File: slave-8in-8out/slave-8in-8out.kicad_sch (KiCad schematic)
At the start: 47 parts, among them J1 Conn_01x06_Male, J2 Screw_Terminal_01x02, J3 Conn_01x06_Female, J4 Screw_Terminal_01x04, J5 Screw_Terminal_01x04, J6 Screw_Terminal_01x04, J7 Screw_Terminal_01x04, J8 Conn_01x10_Female, J9 Screw_Terminal_01x02, SW1 SW_DIP_x03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

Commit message: update slave-8in-8out routing
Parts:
- D1, D2, D3, D4, D5, D6, D7, D8: footprint Resistor_SMD:R_0805_2012Metric -> LED_SMD:LED_0805_2012Metric
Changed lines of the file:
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@@
     (property "Reference" "D1" (id 0) (at 127.381 85.09 0))
     (property "Value" "LED" (id 1) (at 127.381 87.63 0))
-    (property "Footprint" "Resistor_SMD:R_0805_2012Metric" (id 2) (at 127 92.71 0)
+    (property "Footprint" "LED_SMD:LED_0805_2012Metric" (id 2) (at 127 92.71 0)
       (effects (font (size 1.27 1.27)) hide)
     )
@@
     (property "Reference" "D2" (id 0) (at 127.381 93.98 0))
     (property "Value" "LED" (id 1) (at 127.381 96.52 0))
-    (property "Footprint" "Resistor_SMD:R_0805_2012Metric" (id 2) (at 127 101.6 0)
+    (property "Footprint" "LED_SMD:LED_0805_2012Metric" (id 2) (at 127 101.6 0)
       (effects (font (size 1.27 1.27)) hide)
     )
@@
     (property "Reference" "D3" (id 0) (at 127.381 102.87 0))
     (property "Value" "LED" (id 1) (at 127.381 105.41 0))
-    (property "Footprint" "Resistor_SMD:R_0805_2012Metric" (id 2) (at 127 110.49 0)
+    (property "Footprint" "LED_SMD:LED_0805_2012Metric" (id 2) (at 127 110.49 0)
       (effects (font (size 1.27 1.27)) hide)
     )
@@
     (property "Reference" "D4" (id 0) (at 127.381 111.76 0))
     (property "Value" "LED" (id 1) (at 127.381 114.3 0))
-    (property "Footprint" "Resistor_SMD:R_0805_2012Metric" (id 2) (at 127 119.38 0)
+    (property "Footprint" "LED_SMD:LED_0805_2012Metric" (id 2) (at 127 119.38 0)
       (effects (font (size 1.27 1.27)) hide)
     )
@@
     (property "Reference" "D5" (id 0) (at 127.381 120.65 0))
     (property "Value" "LED" (id 1) (at 127.381 123.19 0))
-    (property "Footprint" "Resistor_SMD:R_0805_2012Metric" (id 2) (at 127 128.27 0)
+    (property "Footprint" "LED_SMD:LED_0805_2012Metric" (id 2) (at 127 128.27 0)
       (effects (font (size 1.27 1.27)) hide)
     )
@@
     (property "Reference" "D6" (id 0) (at 127.381 129.54 0))
     (property "Value" "LED" (id 1) (at 127.381 132.08 0))
-    (property "Footprint" "Resistor_SMD:R_0805_2012Metric" (id 2) (at 127 137.16 0)
+    (property "Footprint" "LED_SMD:LED_0805_2012Metric" (id 2) (at 127 137.16 0)
       (effects (font (size 1.27 1.27)) hide)
     )
@@
     (property "Reference" "D7" (id 0) (at 127.381 138.43 0))
     (property "Value" "LED" (id 1) (at 127.381 140.97 0))
-    (property "Footprint" "Resistor_SMD:R_0805_2012Metric" (id 2) (at 127 146.05 0)
+    (property "Footprint" "LED_SMD:LED_0805_2012Metric" (id 2) (at 127 146.05 0)
       (effects (font (size 1.27 1.27)) hide)
     )
@@
     (property "Reference" "D8" (id 0) (at 127.381 147.32 0))
     (property "Value" "LED" (id 1) (at 127.381 149.86 0))
-    (property "Footprint" "Resistor_SMD:R_0805_2012Metric" (id 2) (at 127 154.94 0)
+    (property "Footprint" "LED_SMD:LED_0805_2012Metric" (id 2) (at 127 154.94 0)
       (effects (font (size 1.27 1.27)) hide)
     )
@@
     )
     (path "/1130ddb6-2676-4fcc-a4bc-f126e5a4cfda"
-      (reference "D1") (unit 1) (value "LED") (footprint "Resistor_SMD:R_0805_2012Metric")
+      (reference "D1") (unit 1) (value "LED") (footprint "LED_SMD:LED_0805_2012Metric")
     )
     (path "/c04a3c0f-1c24-409e-afcf-fa43ae33581a"
-      (reference "D2") (unit 1) (value "LED") (footprint "Resistor_SMD:R_0805_2012Metric")
+      (reference "D2") (unit 1) (value "LED") (footprint "LED_SMD:LED_0805_2012Metric")
     )
     (path "/05aa0f77-6513-48a5-a5d4-97e427a3a373"
-      (reference "D3") (unit 1) (value "LED") (footprint "Resistor_SMD:R_0805_2012Metric")
+      (reference "D3") (unit 1) (value "LED") (footprint "LED_SMD:LED_0805_2012Metric")
     )
     (path "/eaa25c40-d6da-42ff-9377-01443632b7c7"
-      (reference "D4") (unit 1) (value "LED") (footprint "Resistor_SMD:R_0805_2012Metric")
+      (reference "D4") (unit 1) (value "LED") (footprint "LED_SMD:LED_0805_2012Metric")
     )
     (path "/504d2596-392e-4876-87b1-2ae7254e5876"
-      (reference "D5") (unit 1) (value "LED") (footprint "Resistor_SMD:R_0805_2012Metric")
+      (reference "D5") (unit 1) (value "LED") (footprint "LED_SMD:LED_0805_2012Metric")
     )
     (path "/4c0f8732-eaad-43c0-94bc-9e71f4a27432"
-      (reference "D6") (unit 1) (value "LED") (footprint "Resistor_SMD:R_0805_2012Metric")
+      (reference "D6") (unit 1) (value "LED") (footprint "LED_SMD:LED_0805_2012Metric")
     )
     (path "/f4af2212-81b4-4a8c-a4ec-5b893151c71f"
-      (reference "D7") (unit 1) (value "LED") (footprint "Resistor_SMD:R_0805_2012Metric")
+      (reference "D7") (unit 1) (value "LED") (footprint "LED_SMD:LED_0805_2012Metric")
     )
     (path "/20c2455c-6d84-4646-a0f8-565d2e8a91c0"
-      (reference "D8") (unit 1) (value "LED") (footprint "Resistor_SMD:R_0805_2012Metric")
+      (reference "D8") (unit 1) (value "LED") (footprint "LED_SMD:LED_0805_2012Metric")
     )
     (path "/00000000-0000-0000-0000-0000601f3a35/b0a7a218-e2f0-4093-b668-da203b2eafe3"
-      (reference "D9") (unit 1) (value "LED") (footprint "Resistor_SMD:R_0805_2012Metric")
+      (reference "D9") (unit 1) (value "LED") (footprint "LED_SMD:LED_0805_2012Metric")
     )
     (path "/00000000-0000-0000-0000-0000601f3f45/b0a7a218-e2f0-4093-b668-da203b2eafe3"
-      (reference "D11") (unit 1) (value "LED") (footprint "Resistor_SMD:R_0805_2012Metric")
+      (reference "D11") (unit 1) (value "LED") (footprint "LED_SMD:LED_0805_2012Metric")
     )
     (path "/00000000-0000-0000-0000-0000601fb64e/b0a7a218-e2f0-4093-b668-da203b2eafe3"
-      (reference "D13") (unit 1) (value "LED") (footprint "Resistor_SMD:R_0805_2012Metric")
+      (reference "D13") (unit 1) (value "LED") (footprint "LED_SMD:LED_0805_2012Metric")
     )
     (path "/00000000-0000-0000-0000-0000601f54fa/b0a7a218-e2f0-4093-b668-da203b2eafe3"
-      (reference "D15") (unit 1) (value "LED") (footprint "Resistor_SMD:R_0805_2012Metric")
+      (reference "D15") (unit 1) (value "LED") (footprint "LED_SMD:LED_0805_2012Metric")
     )
     (path "/00000000-0000-0000-0000-0000601f5635/b0a7a218-e2f0-4093-b668-da203b2eafe3"
-      (reference "D17") (unit 1) (value "LED") (footprint "Resistor_SMD:R_0805_2012Metric")
+      (reference "D17") (unit 1) (value "LED") (footprint "LED_SMD:LED_0805_2012Metric")
     )
     (path "/00000000-0000-0000-0000-0000601f5761/b0a7a218-e2f0-4093-b668-da203b2eafe3"
-      (reference "D19") (unit 1) (value "LED") (footprint "Resistor_SMD:R_0805_2012Metric")
+      (reference "D19") (unit 1) (value "LED") (footprint "LED_SMD:LED_0805_2012Metric")
     )
     (path "/00000000-0000-0000-0000-0000601f5881/b0a7a218-e2f0-4093-b668-da203b2eafe3"
-      (reference "D21") (unit 1) (value "LED") (footprint "Resistor_SMD:R_0805_2012Metric")
+      (reference "D21") (unit 1) (value "LED") (footprint "LED_SMD:LED_0805_2012Metric")
     )
     (path "/00000000-0000-0000-0000-0000601f5cf2/b0a7a218-e2f0-4093-b668-da203b2eafe3"
-      (reference "D23") (unit 1) (value "LED") (footprint "Resistor_SMD:R_0805_2012Metric")
+      (reference "D23") (unit 1) (value "LED") (footprint "LED_SMD:LED_0805_2012Metric")
     )
     (path "/eee10ae1-7e56-41a5-a4ef-cb8260ee8633"

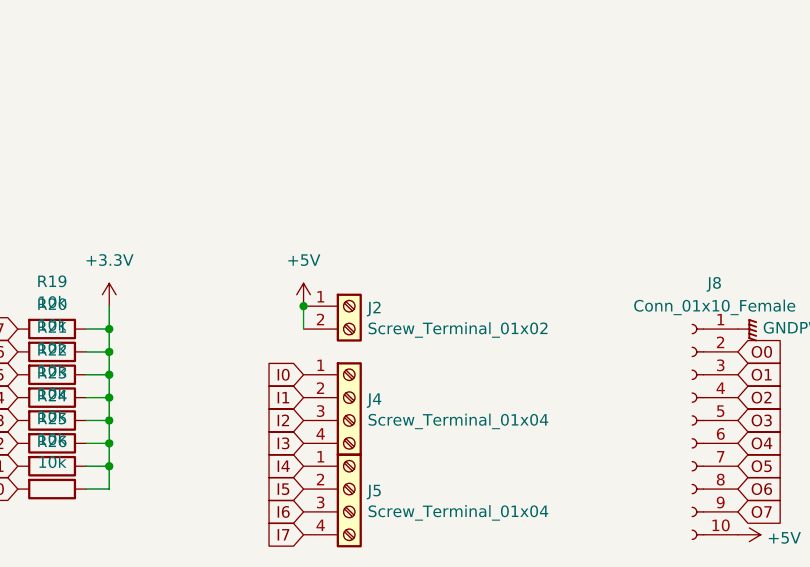
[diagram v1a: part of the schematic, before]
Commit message: update slave-8in-8out routing
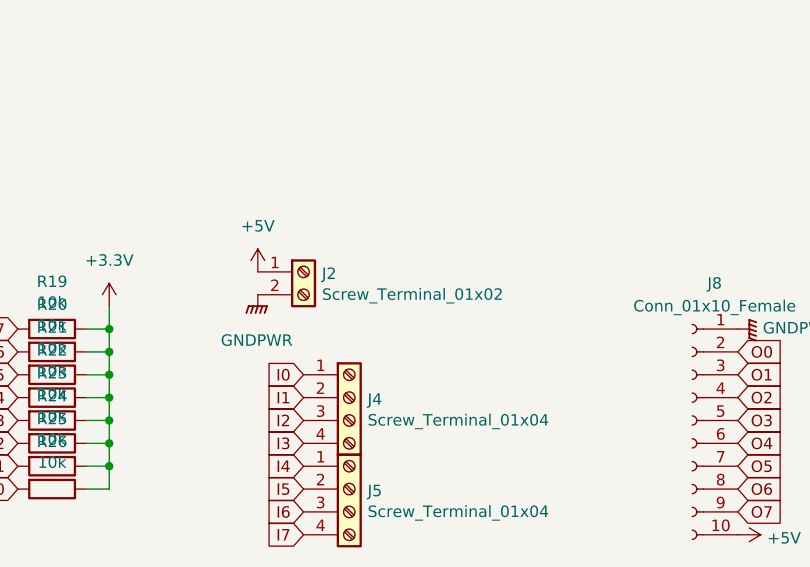
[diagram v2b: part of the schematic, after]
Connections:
- net +5V: no longer J2.2 (Pin_2)
- net GNDPWR: now also J2.2 (Pin_2)
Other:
- moved on the sheet: J2
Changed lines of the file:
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@@
   (junction (at 152.4 64.77) (diameter 0) (color 0 0 0 0))
   (junction (at 152.4 67.31) (diameter 0) (color 0 0 0 0))
-  (junction (at 173.99 49.53) (diameter 0.9144) (color 0 0 0 0))
   (no_connect (at 95.25 43.18))
   (wire (pts (xy 24.13 67.31) (xy 27.94 67.31))
@@
     (stroke (width 0) (type default) (color 0 0 0 0))
   )
-  (wire (pts (xy 173.99 49.53) (xy 173.99 52.07))
-    (stroke (width 0) (type solid) (color 0 0 0 0))
-  )
   (wire (pts (xy 173.99 91.44) (xy 176.53 91.44))
     (stroke (width 0) (type solid) (color 0 0 0 0))
@@
     (pin "1")
   )
-  (symbol (lib_id "power:+5V") (at 173.99 49.53 0) (unit 1)
-    (in_bom yes) (on_board yes) (fields_autoplaced)
-    (property "Reference" "#PWR0139" (id 0) (at 173.99 53.34 0)
-      (effects (font (size 1.27 1.27)) hide)
-    )
-    (property "Value" "+5V" (id 1) (at 173.99 44.45 0))
-    (property "Footprint" "" (id 2) (at 173.99 49.53 0)
-      (effects (font (size 1.27 1.27)) hide)
-    )
-    (property "Datasheet" "" (id 3) (at 173.99 49.53 0)
+  (symbol (lib_id "power:+5V") (at 168.91 45.72 0) (unit 1)
+    (in_bom yes) (on_board yes) (fields_autoplaced)
+    (property "Reference" "#PWR0139" (id 0) (at 168.91 49.53 0)
+      (effects (font (size 1.27 1.27)) hide)
+    )
+    (property "Value" "+5V" (id 1) (at 168.91 40.64 0))
+    (property "Footprint" "" (id 2) (at 168.91 45.72 0)
+      (effects (font (size 1.27 1.27)) hide)
+    )
+    (property "Datasheet" "" (id 3) (at 168.91 45.72 0)
       (effects (font (size 1.27 1.27)) hide)
     )
@@
     )
     (property "Datasheet" "" (id 3) (at 50.8 31.75 0)
+      (effects (font (size 1.27 1.27)) hide)
+    )
+    (pin "1")
+  )
+  (symbol (lib_id "power:GNDPWR") (at 168.91 48.26 0) (unit 1)
+    (in_bom yes) (on_board yes) (fields_autoplaced)
+    (property "Reference" "#PWR?" (id 0) (at 168.91 53.34 0)
+      (effects (font (size 1.27 1.27)) hide)
+    )
+    (property "Value" "GNDPWR" (id 1) (at 168.783 53.34 0))
+    (property "Footprint" "" (id 2) (at 168.91 49.53 0)
+      (effects (font (size 1.27 1.27)) hide)
+    )
+    (property "Datasheet" "" (id 3) (at 168.91 49.53 0)
       (effects (font (size 1.27 1.27)) hide)
     )
@@
     (pin "2")
   )
-  (symbol (lib_id "Connector:Screw_Terminal_01x02") (at 179.07 49.53 0) (unit 1)
-    (in_bom yes) (on_board yes)
-    (property "Reference" "J2" (id 0) (at 181.102 49.7332 0)
-      (effects (font (size 1.27 1.27)) (justify left))
-    )
-    (property "Value" "Screw_Terminal_01x02" (id 1) (at 181.102 52.0446 0)
-      (effects (font (size 1.27 1.27)) (justify left))
-    )
-    (property "Footprint" "TerminalBlock:TerminalBlock_bornier-2_P5.08mm" (id 2) (at 179.07 49.53 0)
-      (effects (font (size 1.27 1.27)) hide)
-    )
-    (property "Datasheet" "~" (id 3) (at 179.07 49.53 0)
-      (effects (font (size 1.27 1.27)) hide)
-    )
-    (property "LCSC" "skip" (id 4) (at 179.07 49.53 0)
+  (symbol (lib_id "Connector:Screw_Terminal_01x02") (at 173.99 45.72 0) (unit 1)
+    (in_bom yes) (on_board yes)
+    (property "Reference" "J2" (id 0) (at 176.022 45.9232 0)
+      (effects (font (size 1.27 1.27)) (justify left))
+    )
+    (property "Value" "Screw_Terminal_01x02" (id 1) (at 176.022 48.2346 0)
+      (effects (font (size 1.27 1.27)) (justify left))
+    )
+    (property "Footprint" "TerminalBlock:TerminalBlock_bornier-2_P5.08mm" (id 2) (at 173.99 45.72 0)
+      (effects (font (size 1.27 1.27)) hide)
+    )
+    (property "Datasheet" "~" (id 3) (at 173.99 45.72 0)
+      (effects (font (size 1.27 1.27)) hide)
+    )
+    (property "LCSC" "skip" (id 4) (at 173.99 45.72 0)
       (effects (font (size 1.27 1.27)) hide)
     )
@@
       (reference "#PWR0141") (unit 1) (value "+3.3V") (footprint "")
     )
+    (path "/d85541cb-1b2b-4244-b900-51571a4724ac"
+      (reference "#PWR?") (unit 1) (value "GNDPWR") (footprint "")
+    )
     (path "/00000000-0000-0000-0000-000060167899"

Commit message: slave-8in-8out-0.2
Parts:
- J8, SW1, SW2: LCSC (none) -> skip
- R11, R12, R13, R14, R15, R16, R17, R18: LCSC C25917 -> C25130
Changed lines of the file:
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@@
   (symbol (lib_id "power:GNDPWR") (at 168.91 48.26 0) (unit 1)
     (in_bom yes) (on_board yes) (fields_autoplaced)
-    (property "Reference" "#PWR?" (id 0) (at 168.91 53.34 0)
+    (property "Reference" "#PWR0142" (id 0) (at 168.91 53.34 0)
       (effects (font (size 1.27 1.27)) hide)
     )
@@
       (effects (font (size 1.27 1.27)) hide)
     )
-    (property "LCSC" "C25917" (id 4) (at 119.38 92.71 90)
+    (property "LCSC" "C25130" (id 4) (at 119.38 92.71 90)
       (effects (font (size 1.27 1.27)) hide)
     )
@@
       (effects (font (size 1.27 1.27)) hide)
     )
-    (property "LCSC" "C25917" (id 4) (at 119.38 101.6 90)
+    (property "LCSC" "C25130" (id 4) (at 119.38 101.6 90)
       (effects (font (size 1.27 1.27)) hide)
     )
@@
       (effects (font (size 1.27 1.27)) hide)
     )
-    (property "LCSC" "C25917" (id 4) (at 119.38 110.49 90)
+    (property "LCSC" "C25130" (id 4) (at 119.38 110.49 90)
       (effects (font (size 1.27 1.27)) hide)
     )
@@
       (effects (font (size 1.27 1.27)) hide)
     )
-    (property "LCSC" "C25917" (id 4) (at 119.38 119.38 90)
+    (property "LCSC" "C25130" (id 4) (at 119.38 119.38 90)
       (effects (font (size 1.27 1.27)) hide)
     )
@@
       (effects (font (size 1.27 1.27)) hide)
     )
-    (property "LCSC" "C25917" (id 4) (at 119.38 128.27 90)
+    (property "LCSC" "C25130" (id 4) (at 119.38 128.27 90)
       (effects (font (size 1.27 1.27)) hide)
     )
@@
       (effects (font (size 1.27 1.27)) hide)
     )
-    (property "LCSC" "C25917" (id 4) (at 119.38 137.16 90)
+    (property "LCSC" "C25130" (id 4) (at 119.38 137.16 90)
       (effects (font (size 1.27 1.27)) hide)
     )
@@
       (effects (font (size 1.27 1.27)) hide)
     )
-    (property "LCSC" "C25917" (id 4) (at 119.38 146.05 90)
+    (property "LCSC" "C25130" (id 4) (at 119.38 146.05 90)
       (effects (font (size 1.27 1.27)) hide)
     )
@@
       (effects (font (size 1.27 1.27)) hide)
     )
-    (property "LCSC" "C25917" (id 4) (at 119.38 154.94 90)
+    (property "LCSC" "C25130" (id 4) (at 119.38 154.94 90)
       (effects (font (size 1.27 1.27)) hide)
     )
@@
       (effects (font (size 1.27 1.27)) hide)
     )
+    (property "LCSC" "skip" (id 4) (at 60.96 49.53 0)
+      (effects (font (size 1.27 1.27)) hide)
+    )
     (pin "1")
     (pin "2")
@@
     )
     (property "Datasheet" "~" (id 3) (at 217.17 62.23 0)
+      (effects (font (size 1.27 1.27)) hide)
+    )
+    (property "LCSC" "skip" (id 4) (at 217.17 62.23 0)
       (effects (font (size 1.27 1.27)) hide)
     )
@@
     )
     (property "Datasheet" "~" (id 3) (at 35.56 72.39 0)
+      (effects (font (size 1.27 1.27)) hide)
+    )
+    (property "LCSC" "skip" (id 4) (at 35.56 72.39 0)
       (effects (font (size 1.27 1.27)) hide)
     )
@@
     )
     (path "/d85541cb-1b2b-4244-b900-51571a4724ac"
-      (reference "#PWR?") (unit 1) (value "GNDPWR") (footprint "")
+      (reference "#PWR0142") (unit 1) (value "GNDPWR") (footprint "")
     )
     (path "/00000000-0000-0000-0000-000060167899"
